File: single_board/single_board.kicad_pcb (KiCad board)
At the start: 4 copper layers, 108.3 x 99.7 mm, 123 parts, among them J11 SPI Debug, J17 BOOTSEL, J2 USB_C_Receptacle_USB2.0_16P, J3 SWD, J30 JST_GH_H, J31 JST_GH_H, J33 JST_GH_H, J34 PB_Vertical, J35 JST_GH_H, J36 JST_GH_H, J37 JST_GH_H, J38 PB_Vertical, J39 PB_Vertical, J40 PB_Vertical, J41 PB_Vertical, J42 PB_Vertical, J43 PB_Vertical, J44 PB_Vertical, J45 PB_Vertical, J46 PB_Vertical, J47 PB_Vertical, J48 PB_Vertical, J49 PB_Vertical, J5 JST-GH, J50 PB_Vertical, J53 PB_Vertical, J6 Conn_01x02, Q1 AO3400A, Q3 AO3401A, SW1 Button, U1 AP2112K-3.3, U3 USBLC6-2SC6, U4 LSM6DSV, U5 STM32G474VBTx, Y2 ABM8-16MHz

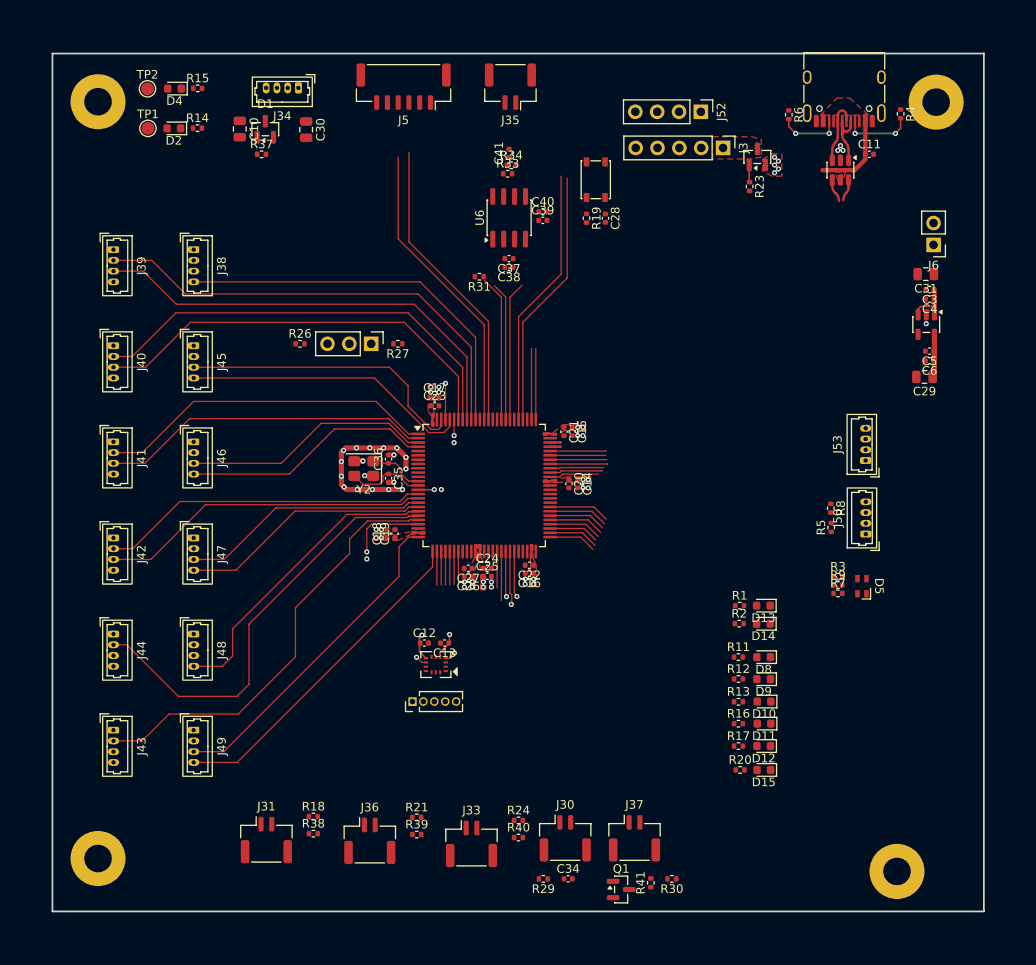
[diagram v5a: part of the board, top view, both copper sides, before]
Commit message: Limit switch topology
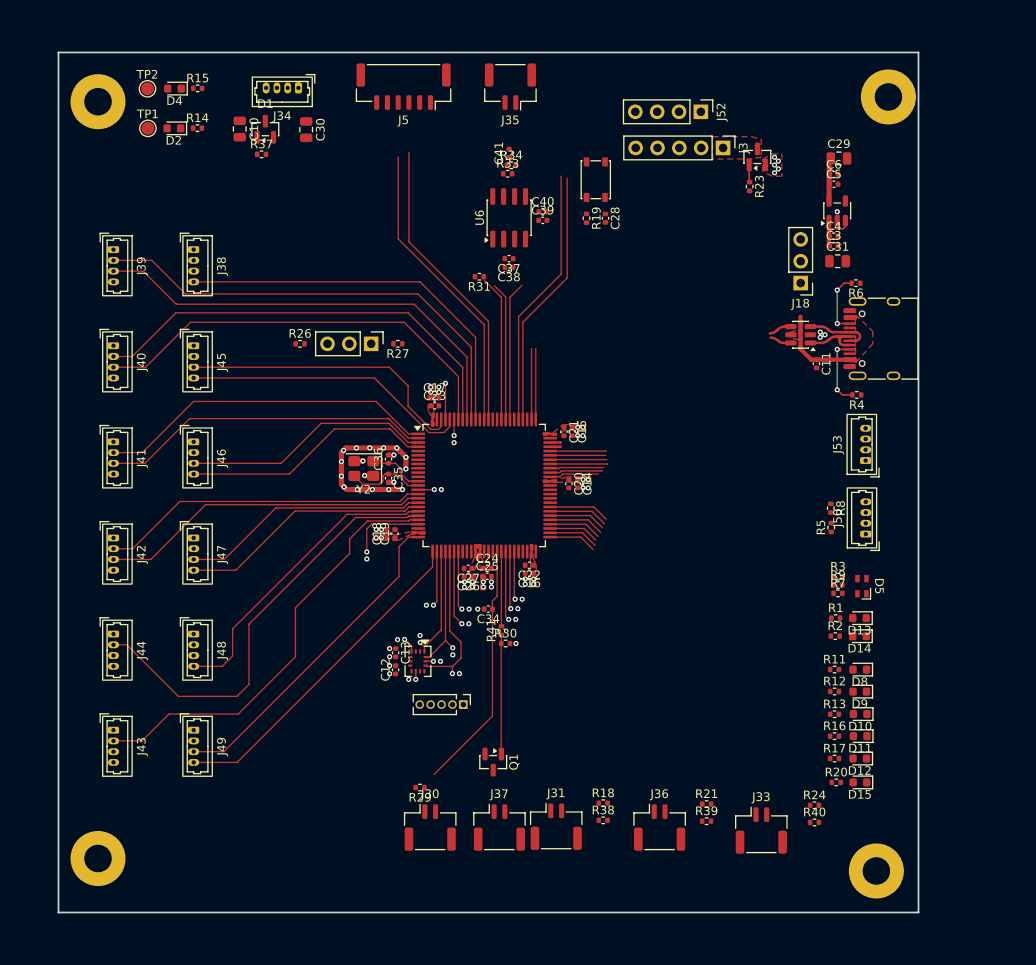
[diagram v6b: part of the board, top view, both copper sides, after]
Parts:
- removed J6: Conn_01x02, Connector_PinHeader_2.54mm:PinHeader_1x02_P2.54mm_Vertical
- added J18: Power, Connector_PinHeader_2.54mm:PinHeader_1x03_P2.54mm_Vertical, F.Cu at (145.6, 60.4)
- moved R24 34.5 mm to (147.2, 121.1)
- moved R40 34.5 mm to (147.2, 123.1)
- moved R41 34.1 mm to (110.8, 100.8)
- moved J31 33.7 mm to (117.2, 123.6)
- moved J33 33.7 mm to (141.0, 124.0)
- moved R18 33.7 mm to (122.6, 120.9)
- moved R21 33.7 mm to (134.7, 121.0)
- moved R38 33.7 mm to (122.6, 122.9)
- moved R39 33.7 mm to (134.7, 123.0)
- moved J36 33.7 mm to (129.2, 123.7)
- moved R30 33.5 mm to (111.3, 102.3), turned to 0 degrees
- moved R4 33.1 mm to (152.1, 73.4), turned to 180 degrees
- moved C34 32.7 mm to (109.3, 98.3), turned to 180 degrees
- moved J2 29.7 mm to (155.3, 66.8), turned to 90 degrees
- moved C29 27.3 mm to (150.1, 45.9), turned to 0 degrees
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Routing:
- net /FSR_ADC: track 4.25 -> 29.0 mm
- net /IMU_NSS: track 3.90 -> 18.3 mm, vias 0 -> 1
- net Net-(Q1-G): track 0.00 -> 13.9 mm
- net /IMU_MOSI: track 3.90 -> 14.7 mm, vias 0 -> 1
- net /IMU_MISO: track 3.90 -> 13.1 mm, vias 0 -> 1
- net v3v3: track 10.3 -> 4.15 mm
- net /INT1: track 5.11 -> 10.5 mm, vias 1 -> 2
- net /IMU_SCK: track 3.90 -> 7.32 mm, vias 0 -> 2
- net /LASER_SIG: track 5.70 -> 8.69 mm
- net /LIM_SW1: track 5.29 -> 8.04 mm
- net /INT2: track 5.14 -> 7.82 mm, vias 1 -> 2
- net GND: vias 44 -> 60
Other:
- board size 108.3 x 99.7 mm -> 100 x 100 mm

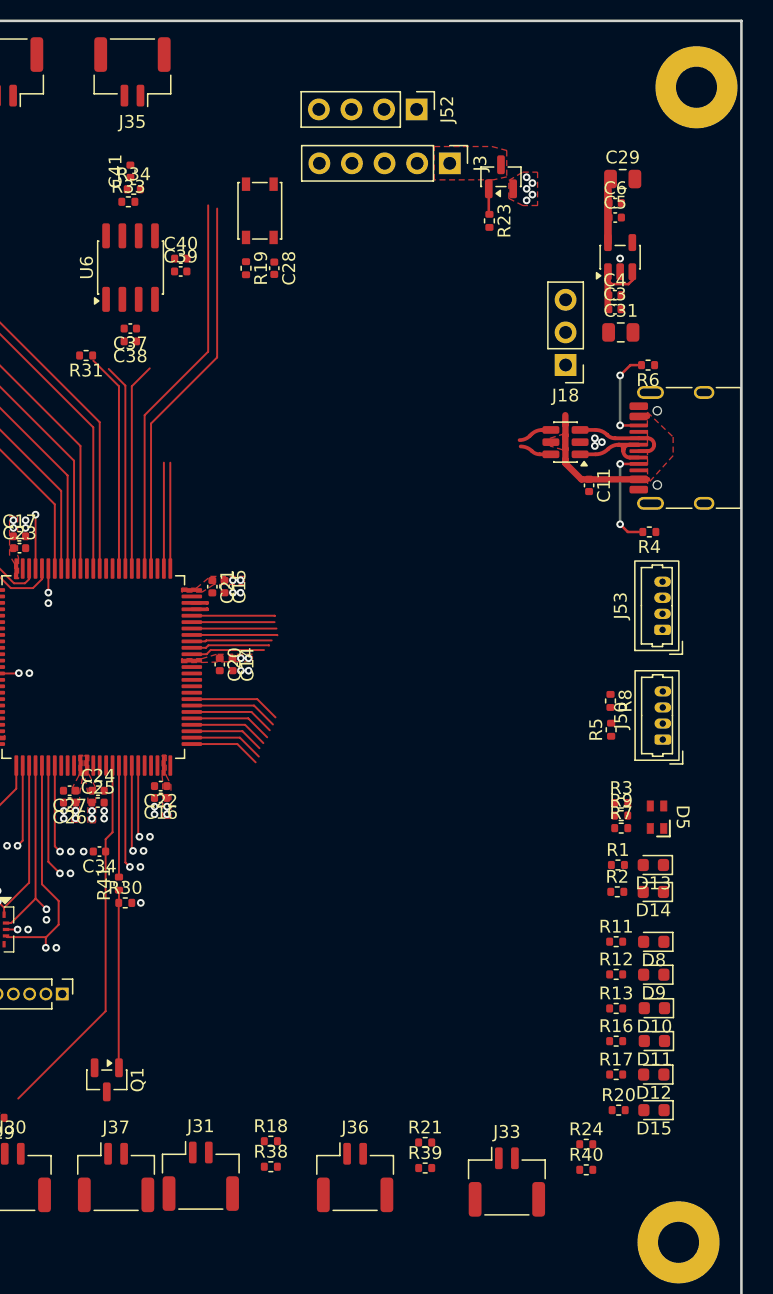
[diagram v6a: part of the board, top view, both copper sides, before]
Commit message: Tri color LED resistors
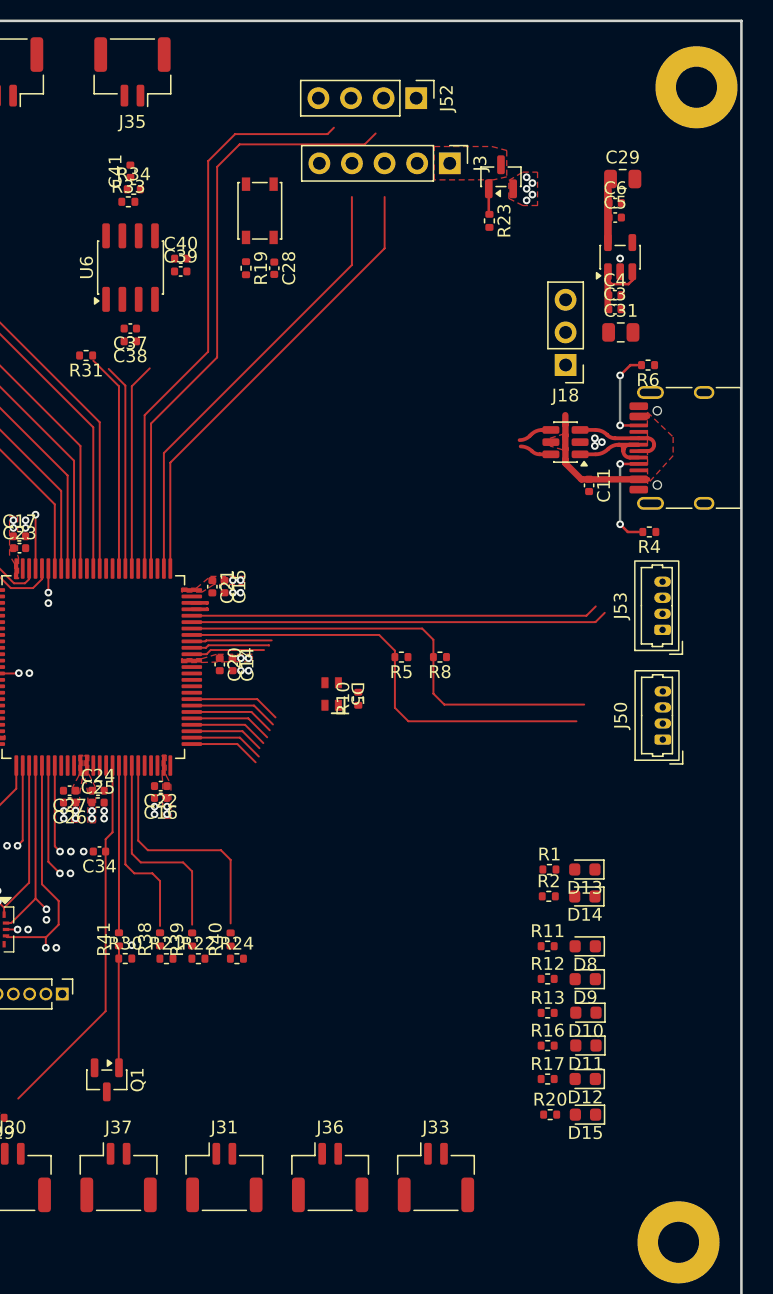
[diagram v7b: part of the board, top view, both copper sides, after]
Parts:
- removed R18, R3, R7, R9: 1k, Resistor_SMD:R_0402_1005Metric
- added R10: 10k, Resistor_SMD:R_0402_1005Metric, F.Cu at (129.4, 86.4)
- added R22: 10k, Resistor_SMD:R_0402_1005Metric, F.Cu at (117.0, 106.7)
- R21, R24: value 1k -> 10k
- moved R40 33.0 mm to (119.5, 105.2), turned to 90 degrees
- moved R24 30.8 mm to (120.0, 106.7)
- moved D5 27.1 mm to (127.4, 86.0)
- moved R39 25.4 mm to (116.5, 105.2), turned to 90 degrees
- moved R21 24.7 mm to (114.5, 106.7)
- moved R38 19.7 mm to (114.0, 105.1), turned to 90 degrees
- moved R5 17.3 mm to (132.8, 83.2), turned to 180 degrees
- moved R8 13.7 mm to (135.8, 83.2), turned to 180 degrees
- moved J33 5.54 mm to (135.5, 123.7)
- moved D10 5.35 mm to (147.2, 110.9)
- moved D11 5.35 mm to (147.2, 113.4)
- moved D12 5.35 mm to (147.1, 116.0)
- moved D13 5.35 mm to (147.1, 99.7)
- moved D8 5.35 mm to (147.1, 105.7)
- moved D9 5.35 mm to (147.1, 108.2)
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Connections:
- D5 pad 1: GND -> Net-(D5-K)
- D5 pad 2: Net-(D5-BA) -> /TRI_LED_B
- D5 pad 3: Net-(D5-RA) -> /TRI_LED_R
- D5 pad 4: Net-(D5-GA) -> /TRI_LED_G
- J31 pad 1: Net-(J31-Pin_1) -> v3v3
- J31 pad 2: GND -> Net-(J31-Pin_2)
- J33 pad 1: Net-(J33-Pin_1) -> v3v3
- J33 pad 2: GND -> Net-(J33-Pin_2)
- J36 pad 1: Net-(J36-Pin_1) -> v3v3
- J36 pad 2: GND -> Net-(J36-Pin_2)
- R21 pad 1: v3v3 -> Net-(J31-Pin_2)
- R21 pad 2: Net-(J36-Pin_1) -> GND
- R24 pad 1: v3v3 -> Net-(J33-Pin_2)
- R24 pad 2: Net-(J33-Pin_1) -> GND
- R38 pad 1: Net-(J31-Pin_1) -> Net-(J31-Pin_2)
- R39 pad 1: Net-(J36-Pin_1) -> Net-(J36-Pin_2)
- R40 pad 1: Net-(J33-Pin_1) -> Net-(J33-Pin_2)
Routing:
- net /I2C_SCL: track 6.60 -> 35.5 mm
- net /I2C_SDA: track 6.69 -> 35.4 mm
- net /SWDIO: track 8.25 -> 35.9 mm
- net /SWCLK: track 8.25 -> 35.0 mm
- net /USART1_TX: track 6.45 -> 32.5 mm
- net /USART1_RX: track 6.49 -> 31.8 mm
- net /USART3_TX: track 30.2 -> 46.9 mm
- net /USART3_RX: track 30.4 -> 44.7 mm
- net /LIM_SW3: track 5.59 -> 18.6 mm, vias 1 -> 0
- net /LIM_SW2: track 6.69 -> 16.3 mm, vias 1 -> 0
- net /LIM_SW1: track 8.04 -> 14.4 mm, vias 1 -> 0
- net Net-(Q1-G): track 13.9 -> 9.52 mm
- net /LASER_SIG: track 8.69 -> 13.0 mm
- net GND: vias 60 -> 57
